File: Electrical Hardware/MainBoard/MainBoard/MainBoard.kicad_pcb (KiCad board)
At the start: 2 copper layers, 49.4 x 51.2 mm, 76 parts, among them J1 SM02B-SRSS-TB_LFSN_, J2 Conn_01x04_Socket, J3 Conn_01x04_Socket, J4 Conn_01x04_Socket, J5 USB_B_Micro, J6 Thermistor, J7 62684-401100ALF, J8 Conn_01x02_Socket, SW1 SW_Push, SW2 SW_Push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

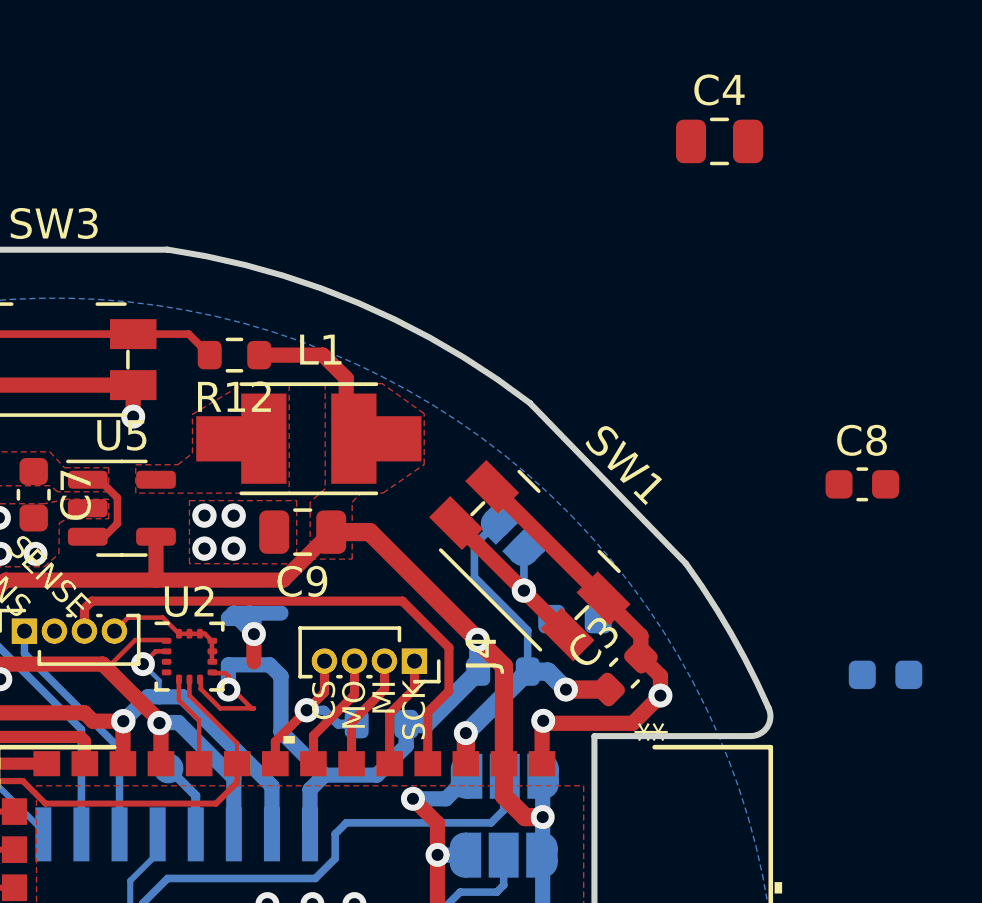
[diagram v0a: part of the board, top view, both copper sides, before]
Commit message: Place all components are they were in previous (original) layout
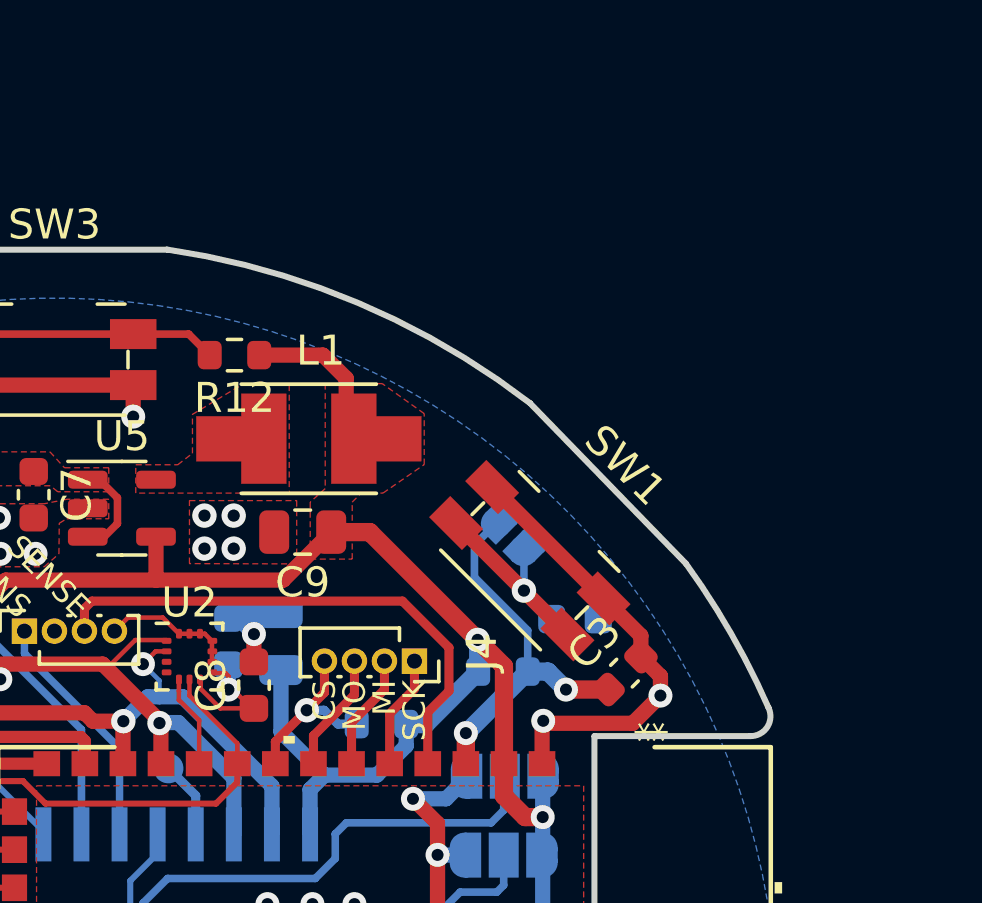
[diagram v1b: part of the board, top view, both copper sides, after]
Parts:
- C4: moved to B.Cu
- moved C4 22.2 mm to (101.3, 38.3), turned to 90 degrees
- moved C6 21.9 mm to (99.5, 38.3), turned to 90 degrees
- moved C8 21.4 mm to (100.4, 39.7), turned to 90 degrees
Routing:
- net +4V4: track 40.4 -> 50.1 mm, vias 3 -> 4
- net /BTN_1: track 38.1 -> 28.4 mm, vias 2 -> 1
- net GND: track 146.0 -> 150.5 mm, vias 31 -> 32
- net /MOSI: track 8.56 -> 3.99 mm, vias 1 -> 0
- added copper zone on F.Cu, net +5V

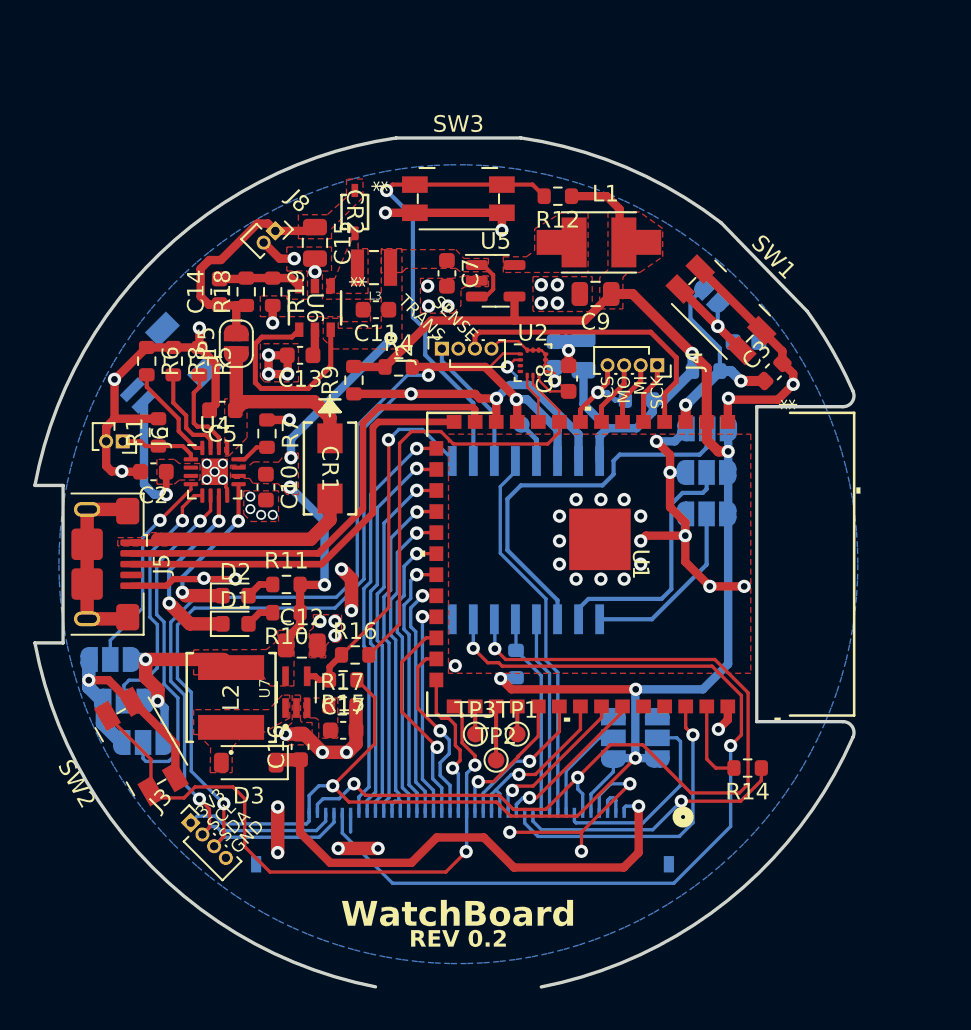
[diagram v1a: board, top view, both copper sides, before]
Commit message: Adjust Silkscreen; Fix board violations and warnings;
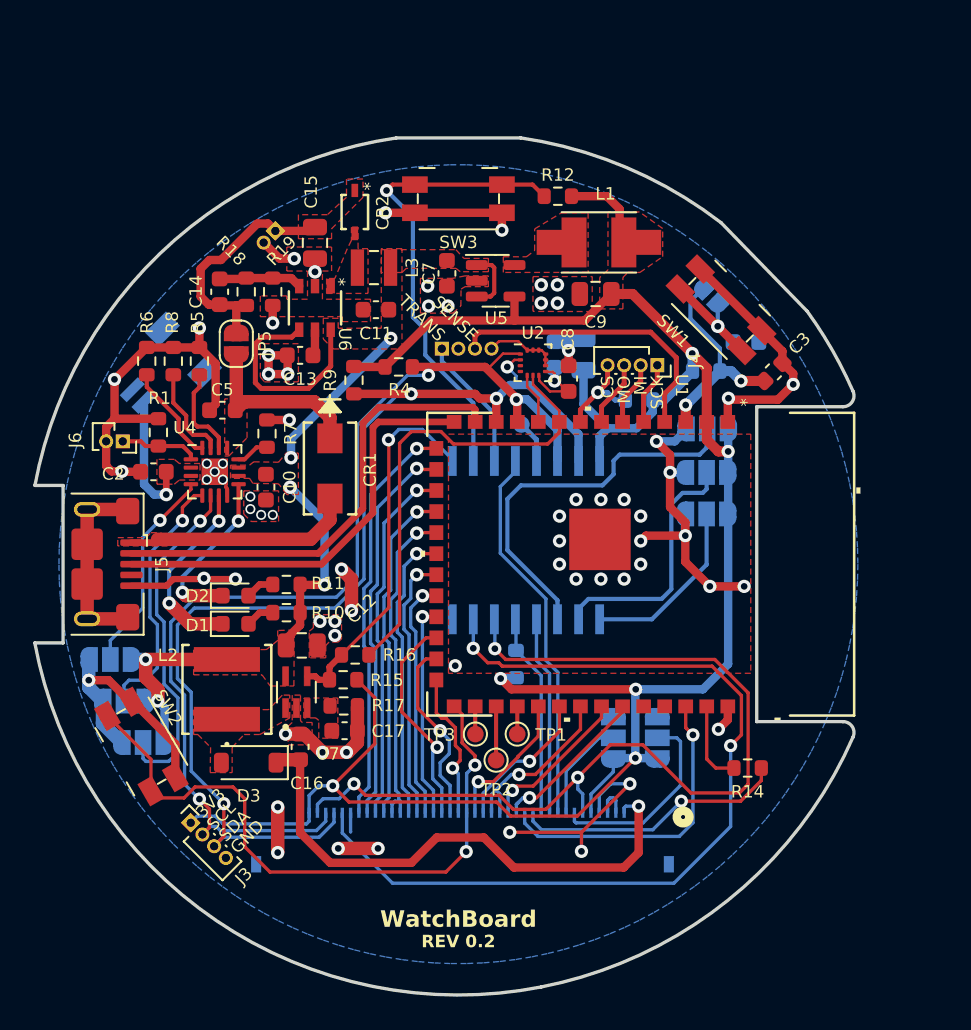
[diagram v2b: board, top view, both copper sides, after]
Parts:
- J2, J8: moved to B.Cu
- moved L2 0.55 mm to (79.8, 58.5)
- moved C17 0.09 mm to (86.9, 61.0)
- moved R17 0.08 mm to (86.8, 59.5)
- turned J2 to -90 degrees
- turned J8 to 135 degrees
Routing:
- net +4V4: track 50.1 -> 50.7 mm, vias 4 -> 6
- net GND: vias 32 -> 68
- net (no net): vias 38 -> 0
- added copper zone on F.Cu, net +3.3V
- added copper zone on F.Cu, net +4V4
- added copper zone on F.Cu, net +5V_IN
- added copper zone on F.Cu, net /LEDK
- added copper zone on F.Cu, net /U5_SW
- added copper zone on F.Cu, net /U6_SW
- added copper zone on F.Cu, net /VBAT
- added copper zone on B.Cu, net GND
- added copper zone on F.Cu, net GND
- added copper zone on F.Cu, net Net-(D3-A)
- removed copper zone on B.Cu, net (none)
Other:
- board size 49.4 x 51.2 mm -> 49.4 x 51.7 mm
